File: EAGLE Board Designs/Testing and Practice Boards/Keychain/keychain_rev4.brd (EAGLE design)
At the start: 27.9 x 27.9 mm, 14 parts, among them J1 USB4110, U1 LM555

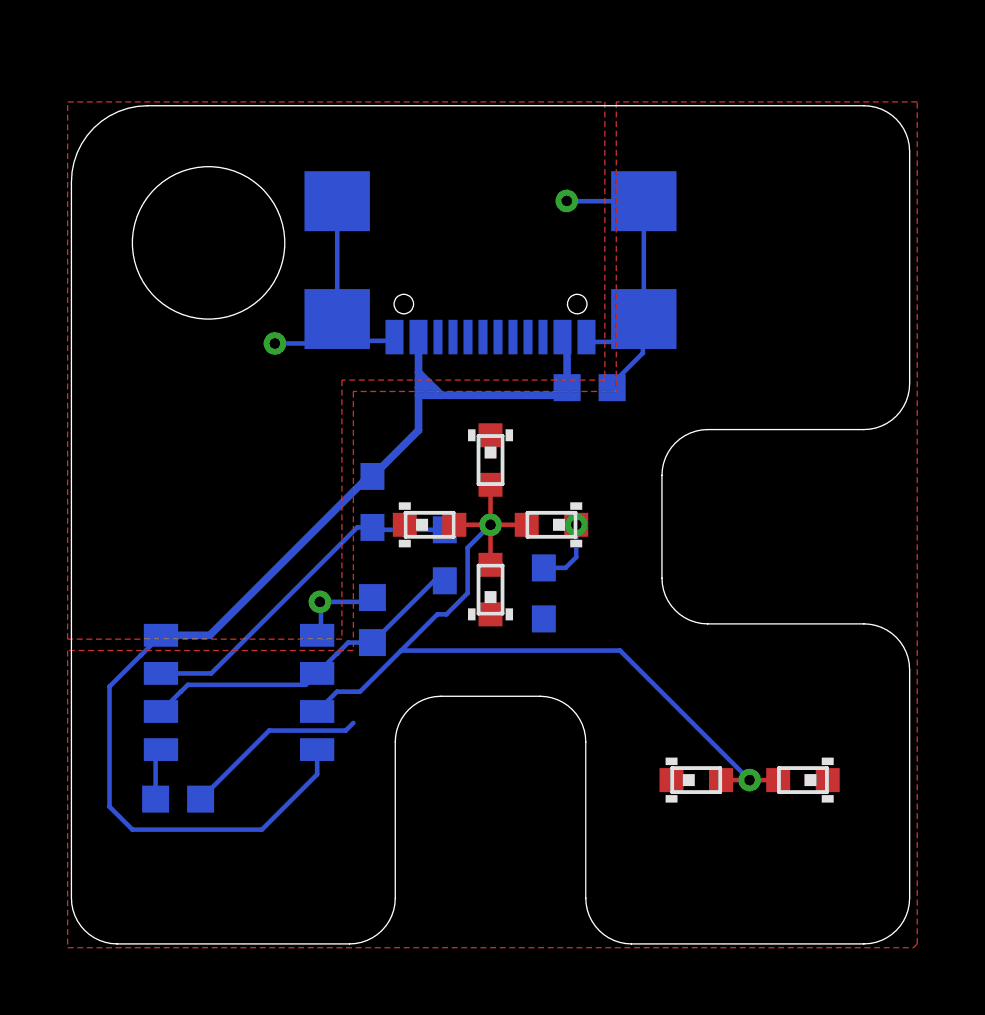
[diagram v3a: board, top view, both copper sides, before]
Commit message: Completed routing
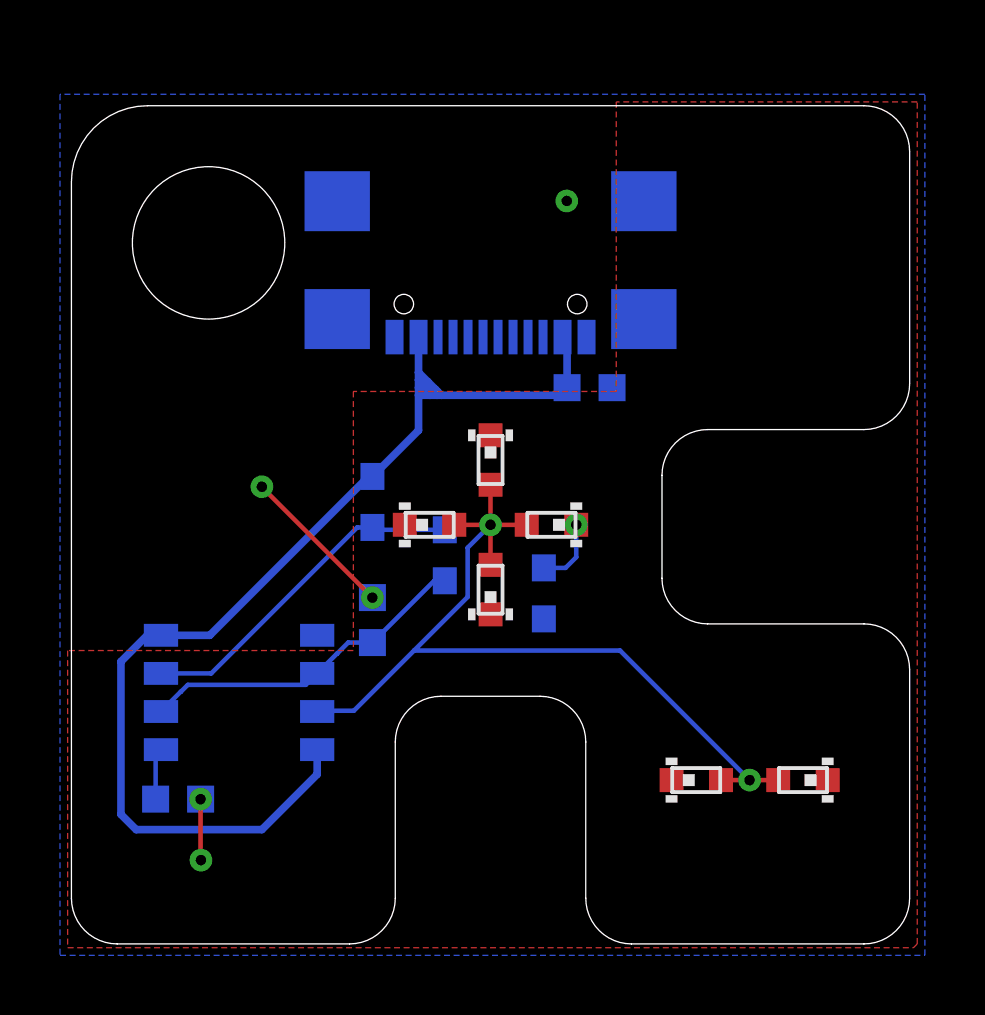
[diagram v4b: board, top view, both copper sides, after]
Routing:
- net GND: track 27.6 -> 9.65 mm, vias 3 -> 5
- added copper zone on layer 16, net GND
- removed copper zone on layer 1, net GND
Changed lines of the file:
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@@
 <contactref element="J1" pad="S$1"/>
 <contactref element="J1" pad="S$2"/>
-<wire x1="4.306" y1="4.826" x2="6.592" y2="7.112" width="0.1524" layer="16"/>
-<wire x1="9.144" y1="7.112" x2="9.398" y2="7.366" width="0.1524" layer="16"/>
-<wire x1="6.592" y1="7.112" x2="9.144" y2="7.112" width="0.1524" layer="16"/>
-<polygon width="0.1524" layer="1">
-<vertex x="-0.127" y="10.16"/>
-<vertex x="-0.127" y="28.067"/>
-<vertex x="17.78" y="28.067"/>
-<vertex x="17.78" y="18.796"/>
-<vertex x="9.017" y="18.796"/>
-<vertex x="9.017" y="10.16"/>
-</polygon>
 <wire x1="8.86" y1="20.828" x2="8.0466" y2="20.0146" width="0.1524" layer="16"/>
-<wire x1="8.0466" y1="20.0146" x2="6.7824" y2="20.0146" width="0.1524" layer="16"/>
-<via x="6.7824" y="20.0146" extent="1-16" drill="0.35"/>
-<wire x1="8.3185" y1="11.3665" x2="8.3185" y2="10.414" width="0.1524" layer="16"/>
 <wire x1="8.1915" y1="10.287" x2="8.3185" y2="10.414" width="0.1524" layer="16"/>
-<wire x1="8.283575" y1="11.401425" x2="8.3185" y2="11.3665" width="0.1524" layer="16"/>
-<via x="8.283575" y="11.401425" extent="1-16" drill="0.35"/>
 <wire x1="10.033" y1="11.545" x2="9.889425" y2="11.401425" width="0.1524" layer="16"/>
-<wire x1="9.889425" y1="11.401425" x2="8.283575" y2="11.401425" width="0.1524" layer="16"/>
-<wire x1="8.86" y1="24.758" x2="8.86" y2="20.828" width="0.1524" layer="16"/>
 <wire x1="10.77" y1="20.228" x2="10.643" y2="20.101" width="0.1524" layer="16"/>
-<wire x1="10.643" y1="20.101" x2="9.363" y2="20.101" width="0.1524" layer="16"/>
 <wire x1="9.363" y1="20.101" x2="9.144" y2="20.32" width="0.1524" layer="16"/>
-<wire x1="19.08" y1="24.758" x2="16.517" y2="24.758" width="0.1524" layer="16"/>
 <wire x1="16.517" y1="24.758" x2="16.51" y2="24.765" width="0.1524" layer="16"/>
 <via x="16.51" y="24.765" extent="1-16" drill="0.35"/>
-<wire x1="19.08" y1="24.758" x2="19.08" y2="20.828" width="0.1524" layer="16"/>
 <wire x1="17.332" y1="20.066" x2="17.17" y2="20.228" width="0.1524" layer="16"/>
-<wire x1="19.05" y1="20.066" x2="17.332" y2="20.066" width="0.1524" layer="16"/>
-<wire x1="19.05" y1="19.697" x2="18.022" y2="18.669" width="0.1524" layer="16"/>
 <wire x1="18.022" y1="18.542" x2="18.022" y2="18.669" width="0.1524" layer="16"/>
-<wire x1="19.05" y1="19.697" x2="19.05" y2="20.066" width="0.1524" layer="16"/>
-<wire x1="10.033" y1="11.545" x2="15.748" y2="10.834" width="0" layer="19" extent="16-16"/>
-<wire x1="9.144" y1="20.32" x2="8.86" y2="20.828" width="0" layer="19" extent="16-16"/>
-<wire x1="9.398" y1="7.366" x2="8.1915" y2="10.287" width="0" layer="19" extent="16-16"/>
+<polygon width="0.1524" layer="16">
+<vertex x="-0.381" y="-0.381"/>
+<vertex x="28.448" y="-0.381"/>
+<vertex x="28.448" y="28.321"/>
+<vertex x="-0.381" y="28.321"/>
+</polygon>
+<via x="4.306" y="4.826" extent="1-16" drill="0.35"/>
+<wire x1="4.306" y1="4.826" x2="4.306" y2="2.806" width="0.1524" layer="1"/>
+<wire x1="4.306" y1="2.806" x2="4.318" y2="2.794" width="0.1524" layer="1"/>
+<via x="4.318" y="2.794" extent="1-16" drill="0.35"/>
+<via x="10.033" y="11.545" extent="1-16" drill="0.35"/>
+<wire x1="10.033" y1="11.545" x2="6.35" y2="15.228" width="0.1524" layer="1"/>
+<wire x1="6.35" y1="15.228" x2="6.35" y2="15.24" width="0.1524" layer="1"/>
+<via x="6.35" y="15.24" extent="1-16" drill="0.35"/>
+<wire x1="8.86" y1="20.828" x2="9.144" y2="20.32" width="0" layer="19" extent="16-16"/>
 </signal>
 <signal name="+5V">
@@
 <wire x1="9.906" y1="15.582" x2="4.611" y2="10.287" width="0.254" layer="16"/>
 <wire x1="4.611" y1="10.287" x2="2.9845" y2="10.287" width="0.254" layer="16"/>
-<wire x1="2.9845" y1="10.287" x2="2.3241" y2="9.6266" width="0.1524" layer="16"/>
-<wire x1="2.3241" y1="9.6266" x2="2.3183125" y2="9.6266" width="0.1524" layer="16"/>
-<wire x1="6.35" y1="3.81" x2="8.1915" y2="5.6515" width="0.1524" layer="16"/>
-<wire x1="8.1915" y1="5.6515" x2="8.1915" y2="6.477" width="0.1524" layer="16"/>
-<wire x1="1.27" y1="8.5782875" x2="1.27" y2="4.572" width="0.1524" layer="16"/>
-<wire x1="1.27" y1="4.572" x2="2.032" y2="3.81" width="0.1524" layer="16"/>
-<wire x1="2.3183125" y1="9.6266" x2="1.27" y2="8.5782875" width="0.1524" layer="16"/>
-<wire x1="2.032" y1="3.81" x2="6.35" y2="3.81" width="0.1524" layer="16"/>
+<wire x1="6.35" y1="3.81" x2="8.1915" y2="5.6515" width="0.254" layer="16"/>
+<wire x1="8.1915" y1="5.6515" x2="8.1915" y2="6.477" width="0.254" layer="16"/>
+<wire x1="1.651" y1="9.41213125" x2="1.651" y2="4.318" width="0.254" layer="16"/>
+<wire x1="1.651" y1="4.318" x2="2.159" y2="3.81" width="0.254" layer="16"/>
+<wire x1="2.159" y1="3.81" x2="6.35" y2="3.81" width="0.254" layer="16"/>
+<wire x1="2.9845" y1="10.287" x2="2.52586875" y2="10.287" width="0.254" layer="16"/>
+<wire x1="2.52586875" y1="10.287" x2="1.651" y2="9.41213125" width="0.254" layer="16"/>
 </signal>
 <signal name="N$1">
@@
 <contactref element="D5" pad="2"/>
 <contactref element="D6" pad="2"/>
-<wire x1="8.1915" y1="7.747" x2="8.8519" y2="8.4074" width="0.1524" layer="16"/>
-<wire x1="8.8519" y1="8.4074" x2="9.6186875" y2="8.4074" width="0.1524" layer="16"/>
-<wire x1="12.1972875" y1="10.986" x2="10.9902875" y2="9.779" width="0.1524" layer="16"/>
-<wire x1="10.95614375" y1="9.74485625" x2="9.6186875" y2="8.4074" width="0.1524" layer="16"/>
+<wire x1="8.1915" y1="7.747" x2="8.2169" y2="7.7724" width="0.1524" layer="16"/>
+<wire x1="8.2169" y1="7.7724" x2="9.4146875" y2="7.7724" width="0.1524" layer="16"/>
+<wire x1="13.208" y1="11.5657125" x2="11.4212875" y2="9.779" width="0.1524" layer="16"/>
 <wire x1="12.763" y1="13.97" x2="13.97" y2="13.97" width="0.1524" layer="1"/>
 <via x="13.97" y="13.97" extent="1-16" drill="0.35"/>
@@
 <wire x1="23.559" y1="5.461" x2="22.606" y2="5.461" width="0.1524" layer="1"/>
 <wire x1="13.97" y1="13.97" x2="13.208" y2="13.208" width="0.1524" layer="16"/>
-<wire x1="10.9902875" y1="9.779" x2="10.95614375" y2="9.74485625" width="0.1524" layer="16"/>
 <wire x1="22.606" y1="5.461" x2="18.288" y2="9.779" width="0.1524" layer="16"/>
-<wire x1="18.288" y1="9.779" x2="10.9902875" y2="9.779" width="0.1524" layer="16"/>
-<wire x1="13.208" y1="13.208" x2="13.208" y2="11.6927125" width="0.1524" layer="16"/>
-<wire x1="13.208" y1="11.6927125" x2="12.5012875" y2="10.986" width="0.1524" layer="16"/>
-<wire x1="12.5012875" y1="10.986" x2="12.1972875" y2="10.986" width="0.1524" layer="16"/>
+<wire x1="18.288" y1="9.779" x2="11.4212875" y2="9.779" width="0.1524" layer="16"/>
+<wire x1="13.208" y1="13.208" x2="13.208" y2="11.5657125" width="0.1524" layer="16"/>
+<wire x1="11.4212875" y1="9.779" x2="9.4146875" y2="7.7724" width="0.1524" layer="16"/>
 </signal>
 </signals>

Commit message: Final update
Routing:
- net GND: track 9.65 -> 4.91 mm, vias 5 -> 2
- added copper zone on layer 1, net GND
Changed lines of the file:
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@@
 <drawing>
 <settings>
-<setting alwaysvectorfont="no"/>
+<setting alwaysvectorfont="yes"/>
 <setting verticaltext="up"/>
 </settings>
@@
 <contactref element="J1" pad="S$1"/>
 <contactref element="J1" pad="S$2"/>
-<wire x1="8.86" y1="20.828" x2="8.0466" y2="20.0146" width="0.1524" layer="16"/>
+<wire x1="8.8115" y1="20.7795" x2="8.0466" y2="20.0146" width="0.1524" layer="16"/>
 <wire x1="8.1915" y1="10.287" x2="8.3185" y2="10.414" width="0.1524" layer="16"/>
 <wire x1="10.033" y1="11.545" x2="9.889425" y2="11.401425" width="0.1524" layer="16"/>
 <wire x1="10.77" y1="20.228" x2="10.643" y2="20.101" width="0.1524" layer="16"/>
 <wire x1="9.363" y1="20.101" x2="9.144" y2="20.32" width="0.1524" layer="16"/>
-<wire x1="16.517" y1="24.758" x2="16.51" y2="24.765" width="0.1524" layer="16"/>
-<via x="16.51" y="24.765" extent="1-16" drill="0.35"/>
 <wire x1="17.332" y1="20.066" x2="17.17" y2="20.228" width="0.1524" layer="16"/>
 <wire x1="18.022" y1="18.542" x2="18.022" y2="18.669" width="0.1524" layer="16"/>
@@
 <vertex x="-0.381" y="28.321"/>
 </polygon>
-<via x="4.306" y="4.826" extent="1-16" drill="0.35"/>
-<wire x1="4.306" y1="4.826" x2="4.306" y2="2.806" width="0.1524" layer="1"/>
-<wire x1="4.306" y1="2.806" x2="4.318" y2="2.794" width="0.1524" layer="1"/>
-<via x="4.318" y="2.794" extent="1-16" drill="0.35"/>
-<via x="10.033" y="11.545" extent="1-16" drill="0.35"/>
-<wire x1="10.033" y1="11.545" x2="6.35" y2="15.228" width="0.1524" layer="1"/>
-<wire x1="6.35" y1="15.228" x2="6.35" y2="15.24" width="0.1524" layer="1"/>
-<via x="6.35" y="15.24" extent="1-16" drill="0.35"/>
+<polygon width="0.1524" layer="1">
+<vertex x="-0.127" y="10.16"/>
+<vertex x="9.017" y="10.16"/>
+<vertex x="9.017" y="18.796"/>
+<vertex x="17.78" y="18.796"/>
+<vertex x="17.78" y="28.067"/>
+<vertex x="-0.127" y="28.067"/>
+</polygon>
+<wire x1="8.86" y1="20.828" x2="8.8115" y2="20.7795" width="0.1524" layer="16"/>
+<via x="8.8115" y="20.7795" extent="1-16" drill="0.35"/>
+<wire x1="10.033" y1="11.545" x2="10.033" y2="11.799" width="0.1524" layer="16"/>
+<wire x1="10.033" y1="11.799" x2="9.132" y2="12.7" width="0.1524" layer="16"/>
+<wire x1="9.132" y1="12.7" x2="8.128" y2="12.7" width="0.1524" layer="16"/>
+<via x="8.128" y="12.7" extent="1-16" drill="0.35"/>
 <wire x1="8.86" y1="20.828" x2="9.144" y2="20.32" width="0" layer="19" extent="16-16"/>
 </signal>
@@
 <wire x1="11.811" y1="18.415" x2="11.684" y2="18.542" width="0.254" layer="16"/>
 <wire x1="11.684" y1="18.542" x2="11.57" y2="18.542" width="0.254" layer="16"/>
-<wire x1="10.033" y1="15.582" x2="9.906" y2="15.582" width="0.254" layer="16"/>
-<wire x1="9.906" y1="15.582" x2="4.611" y2="10.287" width="0.254" layer="16"/>
-<wire x1="4.611" y1="10.287" x2="2.9845" y2="10.287" width="0.254" layer="16"/>
+<wire x1="10.033" y1="15.582" x2="7.62" y2="15.582" width="0.254" layer="16"/>
+<wire x1="2.9845" y1="10.287" x2="2.9845" y2="10.9465" width="0.254" layer="16"/>
+<wire x1="7.62" y1="15.582" x2="2.9845" y2="10.9465" width="0.254" layer="16"/>
 <wire x1="6.35" y1="3.81" x2="8.1915" y2="5.6515" width="0.254" layer="16"/>
 <wire x1="8.1915" y1="5.6515" x2="8.1915" y2="6.477" width="0.254" layer="16"/>
@@
 <contactref element="R1" pad="1"/>
 <contactref element="R2" pad="2"/>
-<wire x1="10.033" y1="13.882" x2="9.525" y2="13.882" width="0.1524" layer="16"/>
-<wire x1="9.525" y1="13.882" x2="4.66" y2="9.017" width="0.1524" layer="16"/>
-<wire x1="4.66" y1="9.017" x2="2.9845" y2="9.017" width="0.1524" layer="16"/>
+<wire x1="10.033" y1="13.882" x2="8.128" y2="13.882" width="0.1524" layer="16"/>
+<wire x1="8.128" y1="13.882" x2="3.263" y2="9.017" width="0.1524" layer="16"/>
+<wire x1="3.263" y1="9.017" x2="2.9845" y2="9.017" width="0.1524" layer="16"/>
 <wire x1="12.446" y1="13.804" x2="10.111" y2="13.804" width="0.1524" layer="16"/>
 <wire x1="10.111" y1="13.804" x2="10.033" y2="13.882" width="0.1524" layer="16"/>
